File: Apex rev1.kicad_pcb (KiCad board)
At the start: 2 copper layers, 9.2 x 5.6 mm, 245 parts, among them IC1 24SN, IC2 FE1.1S, J1 OLED, J2 USB_C2-LAYER, J3 USB_A_SMT_FEMALE, J4 USB_A_SMT_FEMALE, J5 USB_A_SMT_FEMALE, SW1 SW_PUSH, SW2 Rotary_Encoder_Switch, U1 AT90USB1286-MU, X1 12MHz, Y1 8MHz

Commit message: switch layout
layed out switches only
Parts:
- moved MX17 697.3 mm to (46.0, 117.5), turned to 180 degrees
- moved MX1 647.9 mm to (46.0, 88.9), turned to 180 degrees
- moved MX18 630.5 mm to (65.1, 117.5), turned to 180 degrees
- moved MX64 612.1 mm to (57.9, 174.6), turned to 180 degrees
- moved MX23 586.7 mm to (160.3, 117.5), turned to 180 degrees
- moved MX20 575.2 mm to (103.2, 117.5), turned to 180 degrees
- moved MX51 568.5 mm to (53.2, 155.6), turned to 180 degrees
- moved MX2 564.8 mm to (84.1, 88.9), turned to 180 degrees
- moved MX19 563.9 mm to (84.1, 117.5), turned to 180 degrees
- moved MX35 560.5 mm to (74.6, 136.5), turned to 180 degrees
- moved MX36 546.2 mm to (93.7, 136.5), turned to 180 degrees
- moved MX37 543.7 mm to (112.7, 136.5), turned to 180 degrees
- moved MX40 543.7 mm to (169.9, 136.5), turned to 180 degrees
- moved MX25 536.2 mm to (198.4, 117.5), turned to 180 degrees
- moved MX53 534.8 mm to (98.4, 155.6), turned to 180 degrees
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
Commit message: usb layout
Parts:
- C10, C11, C14, C15, C16, C17, C18, D4, F1, IC1, IC2, J2, R10, R11, R12, R16, R22, R5, R6, R7, X1: moved to B.Cu
- moved D80 409.4 mm to (39.7, 203.2)
- moved D37 407.6 mm to (40.5, 142.1)
- moved D20 405.7 mm to (39.7, 126.2)
- moved D4 394.8 mm to (38.9, 100.0), turned to 90 degrees
- moved D21 394.2 mm to (57.9, 126.2)
- moved D81 389.6 mm to (62.7, 196.1)
- moved D22 375.7 mm to (77.8, 126.2)
- moved D88 367.0 mm to (329.4, 202.4)
- moved D55 366.3 mm to (74.6, 164.3)
- moved D5 361.5 mm to (77.8, 97.6)
- moved D56 349.4 mm to (92.1, 164.3)
- moved D87 345.7 mm to (304.0, 203.2)
- moved D6 342.4 mm to (97.6, 98.4)
- moved D57 336.5 mm to (111.1, 164.3)
- moved D86 329.0 mm to (280.2, 203.2)
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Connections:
- MX80 pad 1: COL6 -> COL5
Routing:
- added copper zone on B.Cu, net GND
- added copper zone on F.Cu, net GND
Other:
- board size 9.2 x 5.6 mm -> 372.8 x 146.1 mm

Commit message: Plane add
added ground plane and edge cuts. refined USB placement.
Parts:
- C1, C12, C13, C19, C2, C20, C21, C23, C24, C3, C9, D1, D2, D3, J3, J4, J5, R1, R13, R14, R15, R17, R19, R2, R20, R21, R23, R24, R25, R3, R4, R8, R9, SW1, U1, Y1: moved to B.Cu
- moved R17 259.5 mm to (339.6, 43.8), turned to 180 degrees
- moved R9 245.4 mm to (321.6, 41.0), turned to 270 degrees
- moved C9 238.9 mm to (323.7, 41.1), turned to 270 degrees
- moved C13 236.1 mm to (325.2, 38.4)
- moved C20 220.8 mm to (237.1, 80.5), turned to 270 degrees
- moved D2 195.5 mm to (240.7, 81.8), turned to 90 degrees
- moved C21 188.2 mm to (251.8, 71.5), turned to 180 degrees
- moved R20 177.7 mm to (239.8, 78.9), turned to 90 degrees
- moved R21 175.6 mm to (241.7, 78.9), turned to 90 degrees
- moved R19 163.4 mm to (230.5, 71.5), turned to 180 degrees
- moved R8 146.6 mm to (325.8, 40.8), turned to 90 degrees
- moved C11 128.9 mm to (337.1, 59.5)
- moved J2 128.9 mm to (331.3, 23.7)
- moved C10 128.9 mm to (337.9, 20.7)
- moved C14 128.9 mm to (342.8, 46.8)
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
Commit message: Placed Caps
Arranged decoupling capacitors around MCU and for encoder and OLED
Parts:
- C22, C25, C26, C4, C5, C6, C7, C8, R18, R26, R27, R28, R29: moved to B.Cu
- moved C22 244.5 mm to (325.5, 35.7), turned to 90 degrees
- moved R18 242.5 mm to (325.0, 43.8), turned to 180 degrees
- moved R27 165.2 mm to (372.9, 166.8), turned to 90 degrees
- moved R2 160.2 mm to (330.5, 154.1)
- moved R1 159.5 mm to (330.6, 151.0)
- moved R29 157.8 mm to (374.5, 166.7), turned to 270 degrees
- moved C25 156.8 mm to (375.5, 159.1)
- moved R28 156.4 mm to (374.5, 161.5), turned to 90 degrees
- moved C26 149.0 mm to (375.7, 169.8)
- moved R26 147.9 mm to (372.9, 161.5), turned to 270 degrees
- moved C5 59.1 mm to (443.0, 2.67), turned to 180 degrees
- moved C7 53.1 mm to (447.6, 12.3)
- moved C4 52.9 mm to (437.8, 2.67)
- moved C8 52.6 mm to (453.2, 8.38)
- moved C6 43.7 mm to (447.7, 20.7), turned to 270 degrees
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
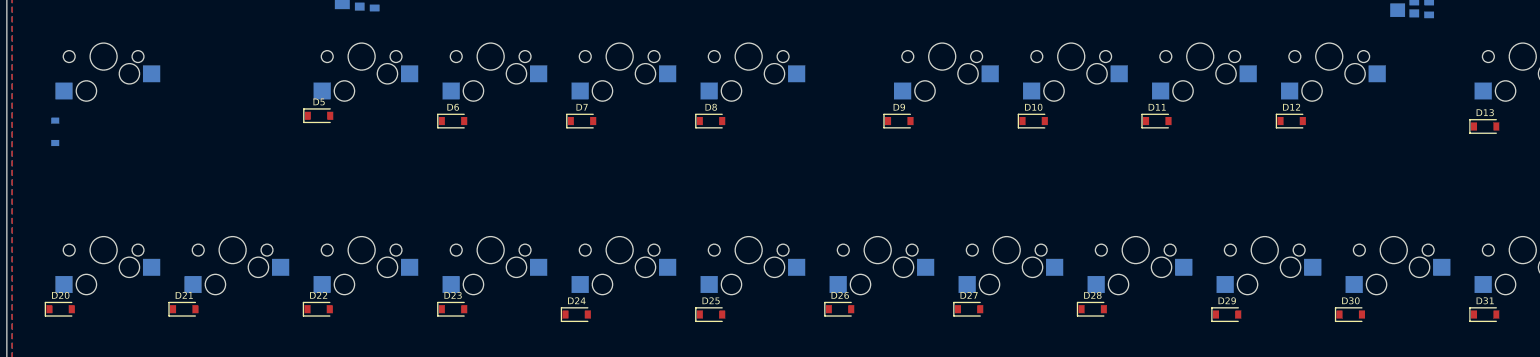
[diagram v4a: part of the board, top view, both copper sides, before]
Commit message: refined diode placement
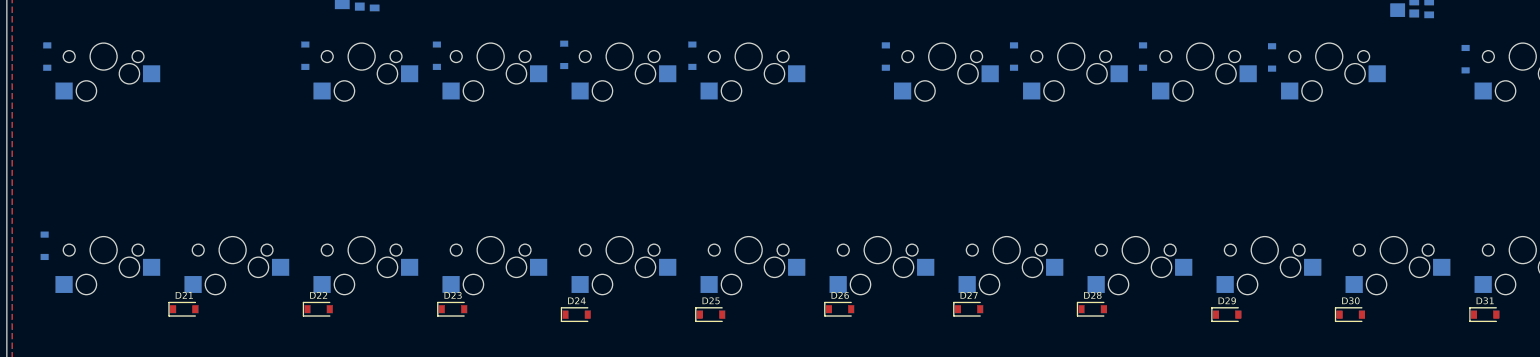
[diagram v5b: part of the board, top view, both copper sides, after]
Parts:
- D10, D11, D12, D13, D20, D5, D6, D7, D8, D9: moved to B.Cu
- moved D4 11.2 mm to (37.7, 88.9), turned to 270 degrees
- moved D13 10.3 mm to (247.1, 89.3), turned to 270 degrees
- moved D7 10.1 mm to (114.0, 88.6), turned to 270 degrees
- moved D8 10.0 mm to (133.0, 88.8), turned to 270 degrees
- moved D10 9.95 mm to (180.5, 88.9), turned to 270 degrees
- moved D6 9.94 mm to (95.2, 88.8), turned to 270 degrees
- moved D12 9.83 mm to (218.6, 89.0), turned to 270 degrees
- moved D11 9.75 mm to (199.5, 88.9), turned to 270 degrees
- moved D9 9.73 mm to (161.5, 88.9), turned to 270 degrees
- moved D20 9.66 mm to (37.3, 116.8), turned to 90 degrees
- moved D5 9.09 mm to (75.8, 88.8), turned to 270 degrees
